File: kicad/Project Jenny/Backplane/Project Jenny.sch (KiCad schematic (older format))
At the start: 54 parts, among them J1 Conn_01x04

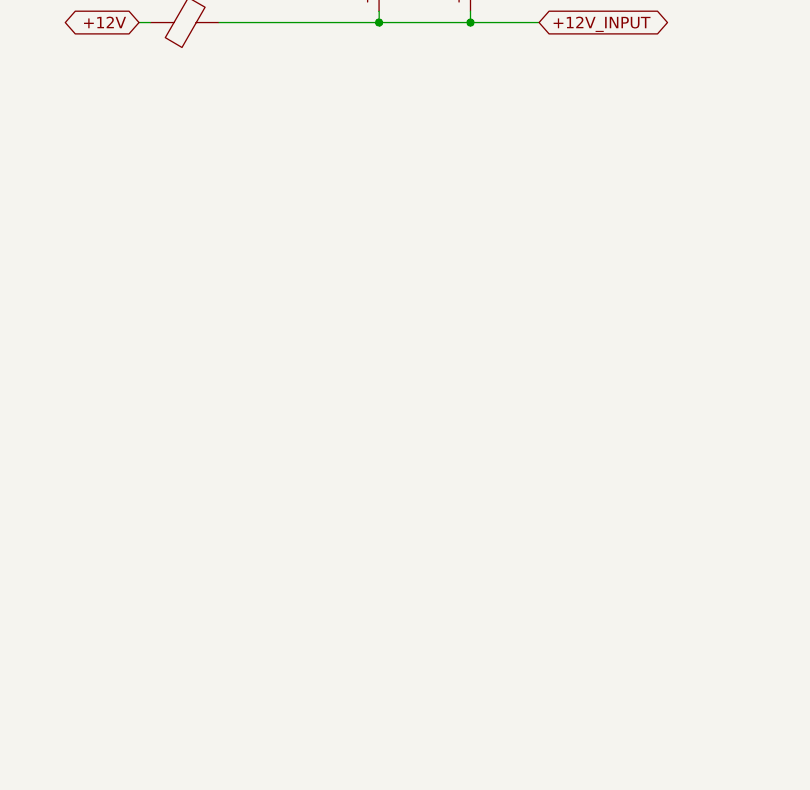
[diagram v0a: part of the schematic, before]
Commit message: add LED lights for +5V and +12V
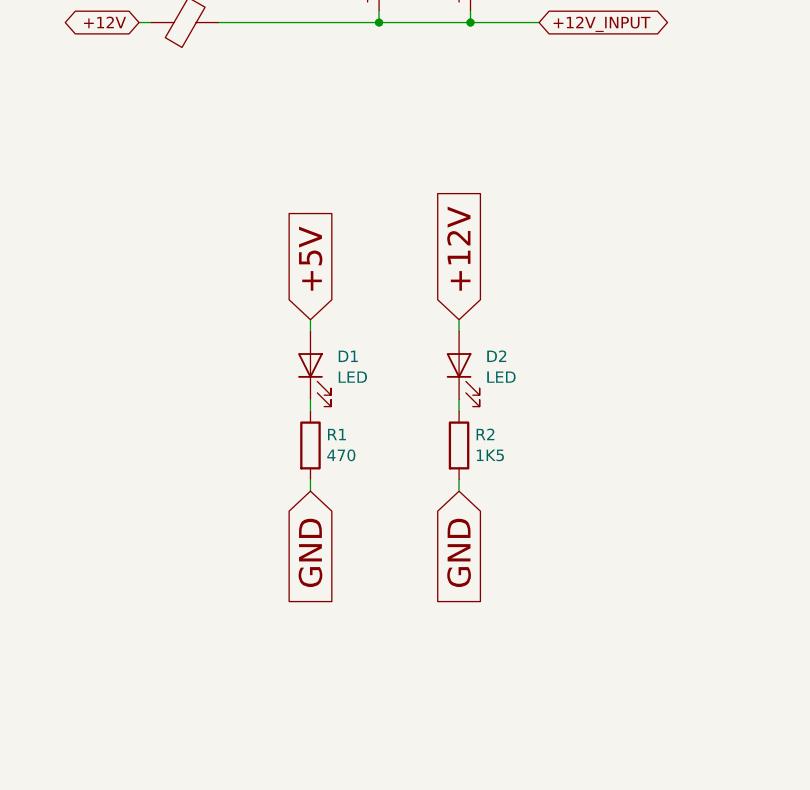
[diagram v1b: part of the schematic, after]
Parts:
- added D1, D2: LED, LED_THT:LED_D5.0mm, symbol Device:LED
- added R1: 470, Resistor_THT:R_Axial_DIN0204_L3.6mm_D1.6mm_P7.62mm_Horizontal, symbol Device:R
- added R2: 1K5, Resistor_THT:R_Axial_DIN0204_L3.6mm_D1.6mm_P7.62mm_Horizontal, symbol Device:R
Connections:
- net +12V: now also D2.2 (A)
- net +5V: now also D1.2 (A)
- net GND: now also R1.2, R2.2
- new net: D1.1 (K), R1.1
- new net: D2.1 (K), R2.1
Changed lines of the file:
@@
 	14800 3500 15500 3500
 Connection ~ 15500 3500
+$Comp
+L Device:LED D1
+U 1 1 6089E366
+P 15200 5000
+F 0 "D1" V 15238 4883 50  0000 R CNN
+F 1 "LED" V 15147 4883 50  0000 R CNN
+F 2 "LED_THT:LED_D5.0mm" H 15200 5000 50  0001 C CNN
+F 3 "~" H 15200 5000 50  0001 C CNN
+	1    15200 5000
+	0    -1   -1   0
+$EndComp
+$Comp
+L Device:LED D2
+U 1 1 6089E548
+P 15850 5000
+F 0 "D2" V 15888 4883 50  0000 R CNN
+F 1 "LED" V 15797 4883 50  0000 R CNN
+F 2 "LED_THT:LED_D5.0mm" H 15850 5000 50  0001 C CNN
+F 3 "~" H 15850 5000 50  0001 C CNN
+	1    15850 5000
+	0    -1   -1   0
+$EndComp
+Wire Wire Line
+	15200 4850 15200 4800
+Wire Wire Line
+	15850 4850 15850 4800
+Text GLabel 15200 4800 1    100  Input ~ 0
++5V
+Text GLabel 15850 4800 1    100  Input ~ 0
++12V
+Wire Wire Line
+	15200 5150 15200 5200
+Wire Wire Line
+	15850 5150 15850 5200
+$Comp
+L Device:R R1
+U 1 1 61026F14
+P 15200 5350
+F 0 "R1" H 15270 5396 50  0000 L CNN
+F 1 "470" H 15270 5305 50  0000 L CNN
+F 2 "Resistor_THT:R_Axial_DIN0204_L3.6mm_D1.6mm_P7.62mm_Horizontal" V 15130 5350 50  0001 C CNN
+F 3 "~" H 15200 5350 50  0001 C CNN
+	1    15200 5350
+	1    0    0    -1
+$EndComp
+$Comp
+L Device:R R2
+U 1 1 61027017
+P 15850 5350
+F 0 "R2" H 15920 5396 50  0000 L CNN
+F 1 "1K5" H 15920 5305 50  0000 L CNN
+F 2 "Resistor_THT:R_Axial_DIN0204_L3.6mm_D1.6mm_P7.62mm_Horizontal" V 15780 5350 50  0001 C CNN
+F 3 "~" H 15850 5350 50  0001 C CNN
+	1    15850 5350
+	1    0    0    -1
+$EndComp
+Wire Wire Line
+	15200 5500 15200 5550
+Wire Wire Line
+	15850 5500 15850 5550
+Text GLabel 15200 5550 3    100  Input ~ 0
+GND
+Text GLabel 15850 5550 3    100  Input ~ 0
+GND
 $EndSCHEMATC
